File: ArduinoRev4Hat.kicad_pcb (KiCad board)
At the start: 2 copper layers, 42.8 x 83.5 mm, 12 parts, among them J1 Conn_01x10_Pin, J10 73099-0, J11 73099-0, J2 Conn_01x08_Pin, J3 Conn_01x04_Pin, J4 Conn_01x04_Pin, J5 Conn_01x04_Pin, J6 73099-0, J7 73099-0, J8 73099-0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

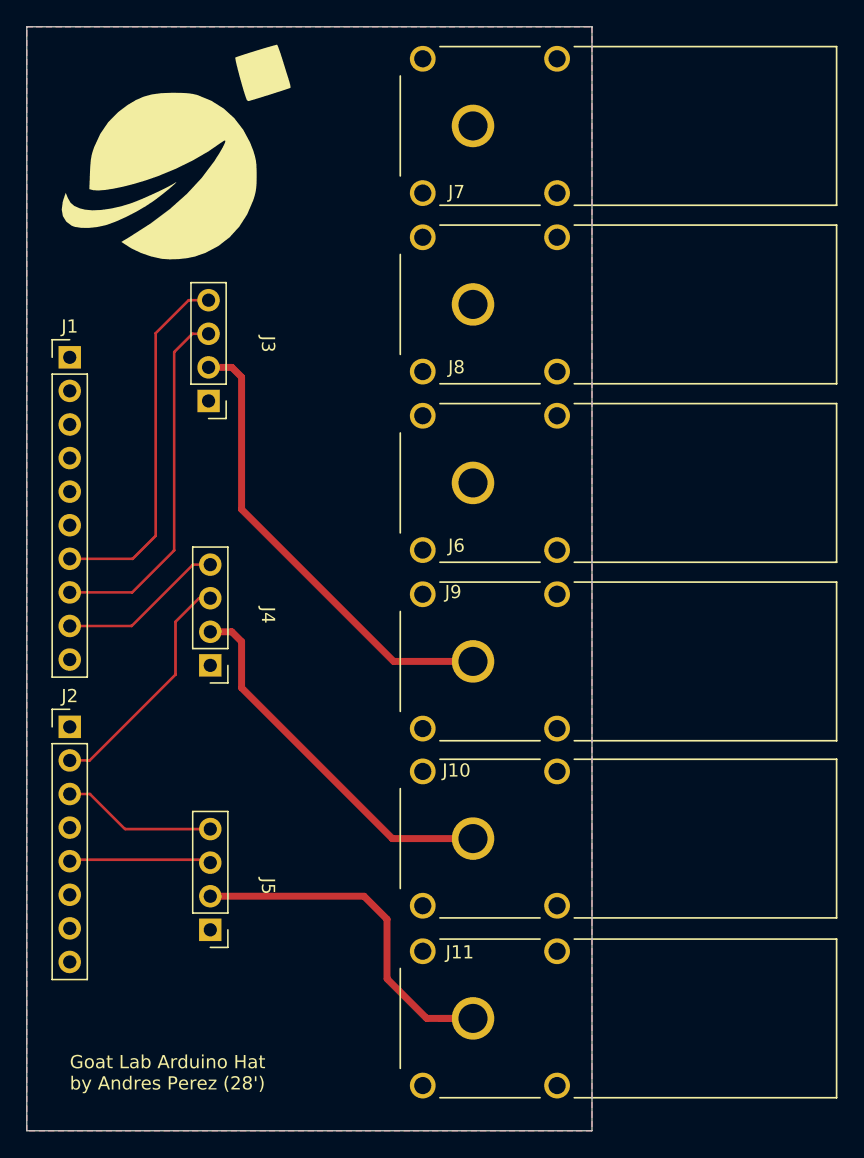
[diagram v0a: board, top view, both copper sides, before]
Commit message: new ground plane
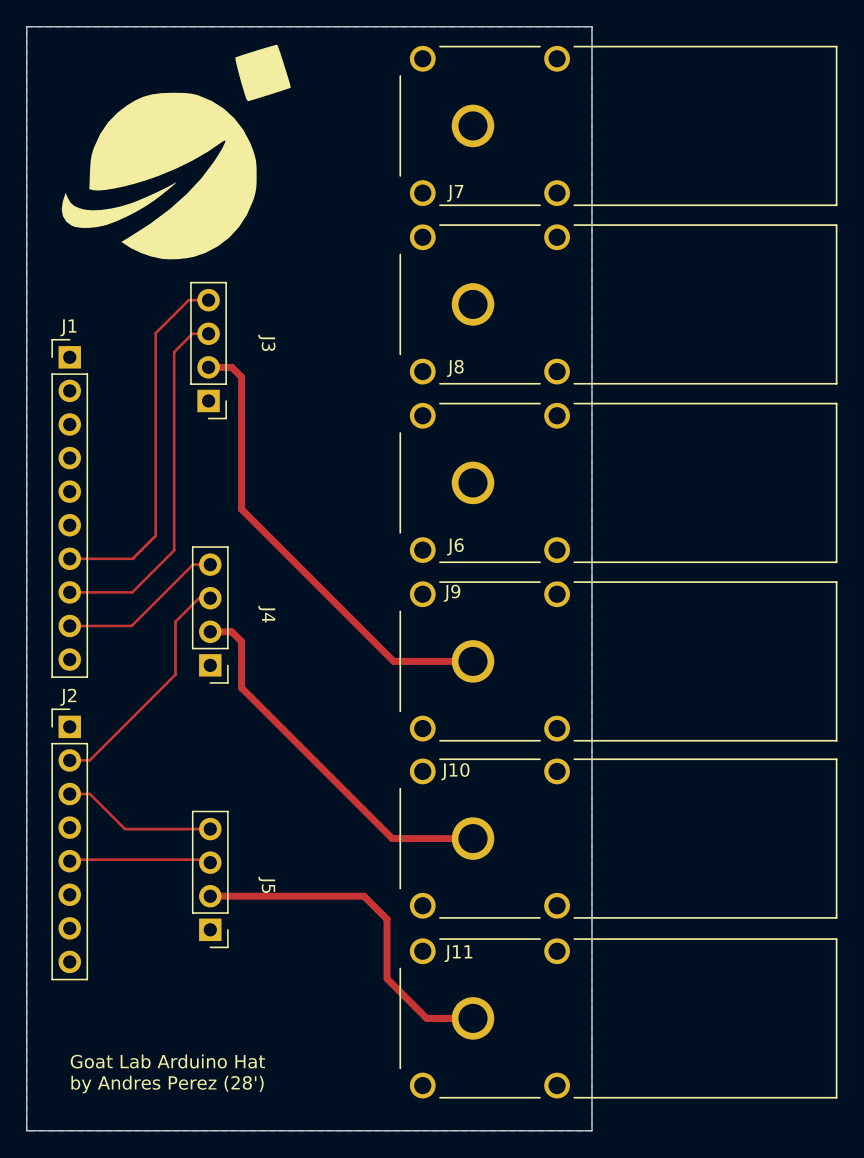
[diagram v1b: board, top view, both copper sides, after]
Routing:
- removed copper zone on F.Cu, net GND
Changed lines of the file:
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@@
 		(net 7)
 		(net_name "GND")
-		(layers "F&B.Cu")
+		(layer "B.Cu")
 		(hatch edge 0.5)
 		(connect_pads
